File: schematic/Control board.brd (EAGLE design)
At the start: 40.3 x 66 mm, 14 parts, among them IC2 ATTINY44AQFN-20

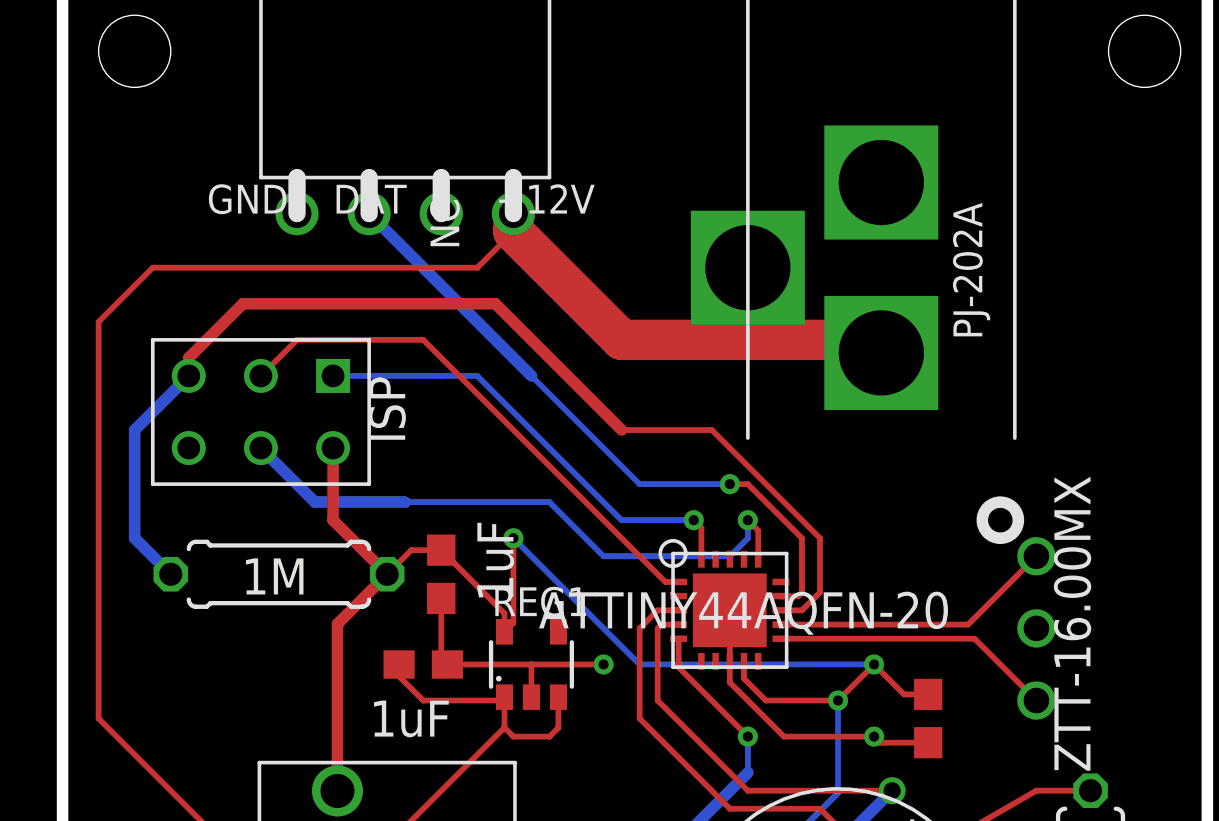
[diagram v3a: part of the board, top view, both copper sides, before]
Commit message: Updated board with QFN-20 microcontroller
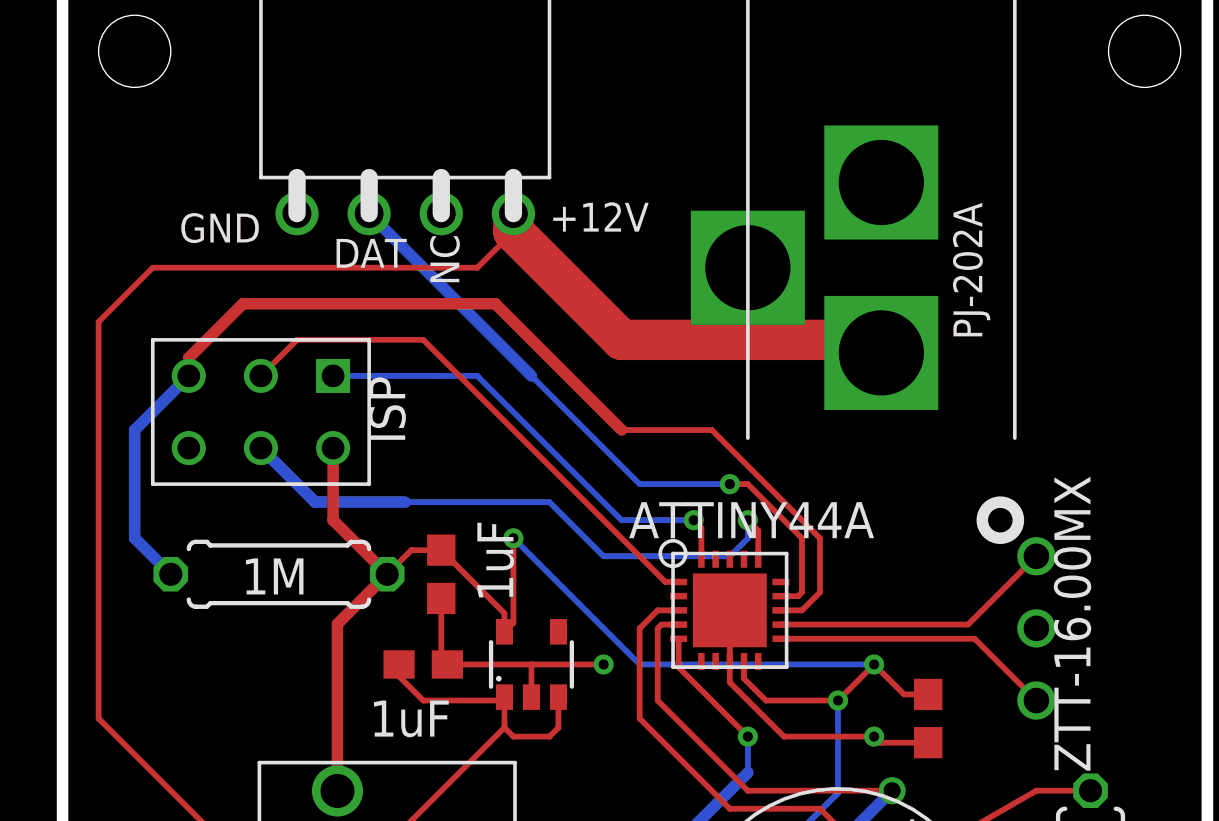
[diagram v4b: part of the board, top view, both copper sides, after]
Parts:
- IC2: value ATTINY44AQFN-20 -> ATTINY44A
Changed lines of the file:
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@@
 <wire x1="40.31" y1="66.03" x2="0" y2="66.03" width="0.4064" layer="20"/>
 <wire x1="0" y1="66.03" x2="0" y2="0" width="0.4064" layer="20"/>
-<text x="15.24" y="57.785" size="1.016" layer="21" font="vector">+12V</text>
-<text x="5.08" y="57.785" size="1.016" layer="21" font="vector">GND</text>
-<text x="9.525" y="57.785" size="1.016" layer="21" font="vector">DAT</text>
-<text x="13.97" y="56.515" size="1.016" layer="21" font="vector" rot="R90">NC</text>
+<text x="17.145" y="57.15" size="1.016" layer="21" font="vector">+12V</text>
+<text x="6.985" y="57.785" size="1.016" layer="21" font="vector" rot="R180">GND</text>
+<text x="9.525" y="55.88" size="1.016" layer="21" font="vector">DAT</text>
+<text x="13.97" y="55.245" size="1.016" layer="21" font="vector" rot="R90">NC</text>
 <circle x="33.02" y="46.99" radius="0.635" width="0.4064" layer="21"/>
 <hole x="2.54" y="63.5" drill="2.54"/>
@@
 </element>
 <element name="CONN1" library="RGB LED project" package="S5440" value="4-PIN-RIGHT-ANGLE" x="12.065" y="57.785" smashed="yes"/>
-<element name="IC2" library="RGB LED project" package="QFN-20" value="ATTINY44AQFN-20" x="23.495" y="43.815" smashed="yes">
-<attribute name="VALUE" x="16.764" y="43.18" size="1.27" layer="21" font="vector" ratio="10"/>
+<element name="IC2" library="RGB LED project" package="QFN-20" value="ATTINY44A" x="23.495" y="43.815" smashed="yes">
+<attribute name="VALUE" x="19.939" y="46.355" size="1.27" layer="21" font="vector" ratio="10"/>
 </element>
 <element name="POW1" library="RGB LED project" package="PJ202A" value="PJ-202A" x="24.13" y="55.88" smashed="yes" rot="R90">
@@
 <attribute name="VALUE" x="31.115" y="33.655" size="1.27" layer="21" font="vector" rot="R90"/>
 </element>
-<element name="REG1" library="RGB LED project" package="SOT-23-5" value="MIC5205" x="16.51" y="41.91"/>
+<element name="REG1" library="RGB LED project" package="SOT-23-5" value="MIC5205" x="16.51" y="41.91" smashed="yes">
+<attribute name="VALUE" x="15.113" y="39.238" size="1.016" layer="27" ratio="10"/>
+</element>
 </elements>
 <signals>

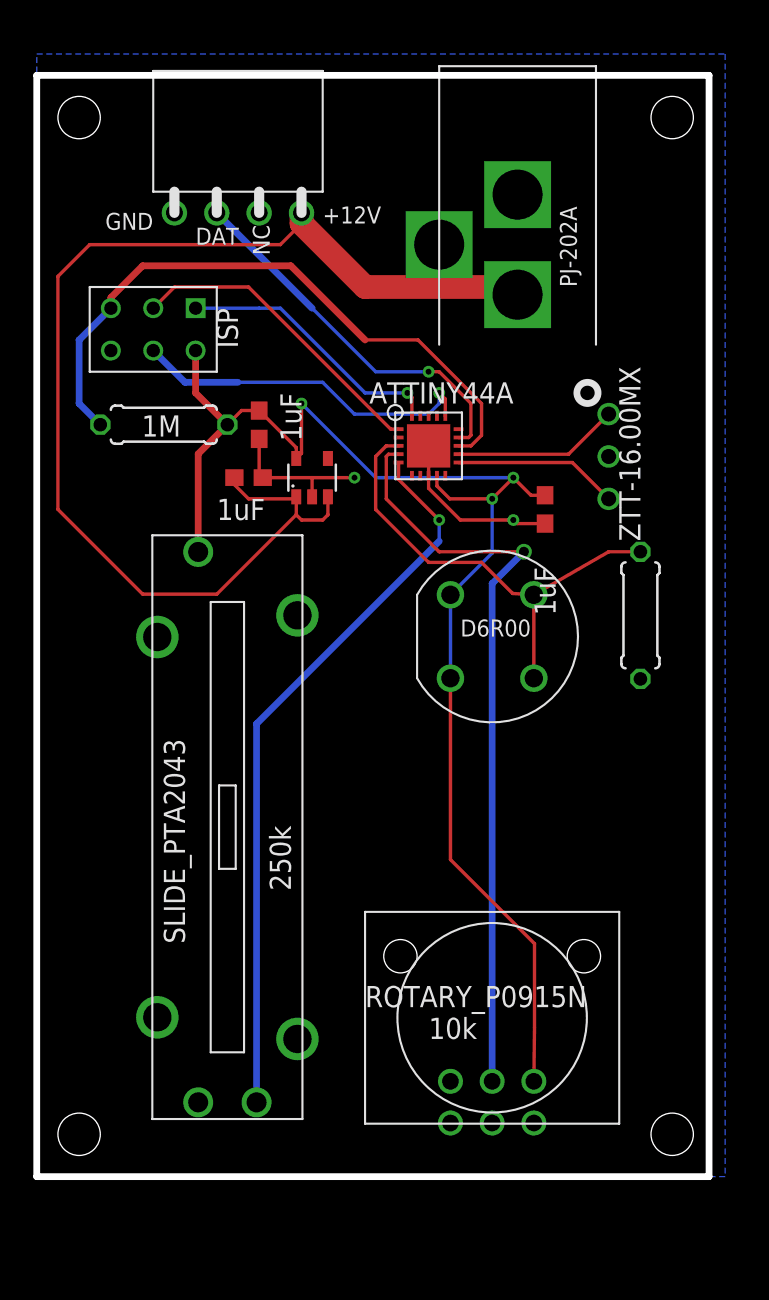
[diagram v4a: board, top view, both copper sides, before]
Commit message: Made the circuit board more compact
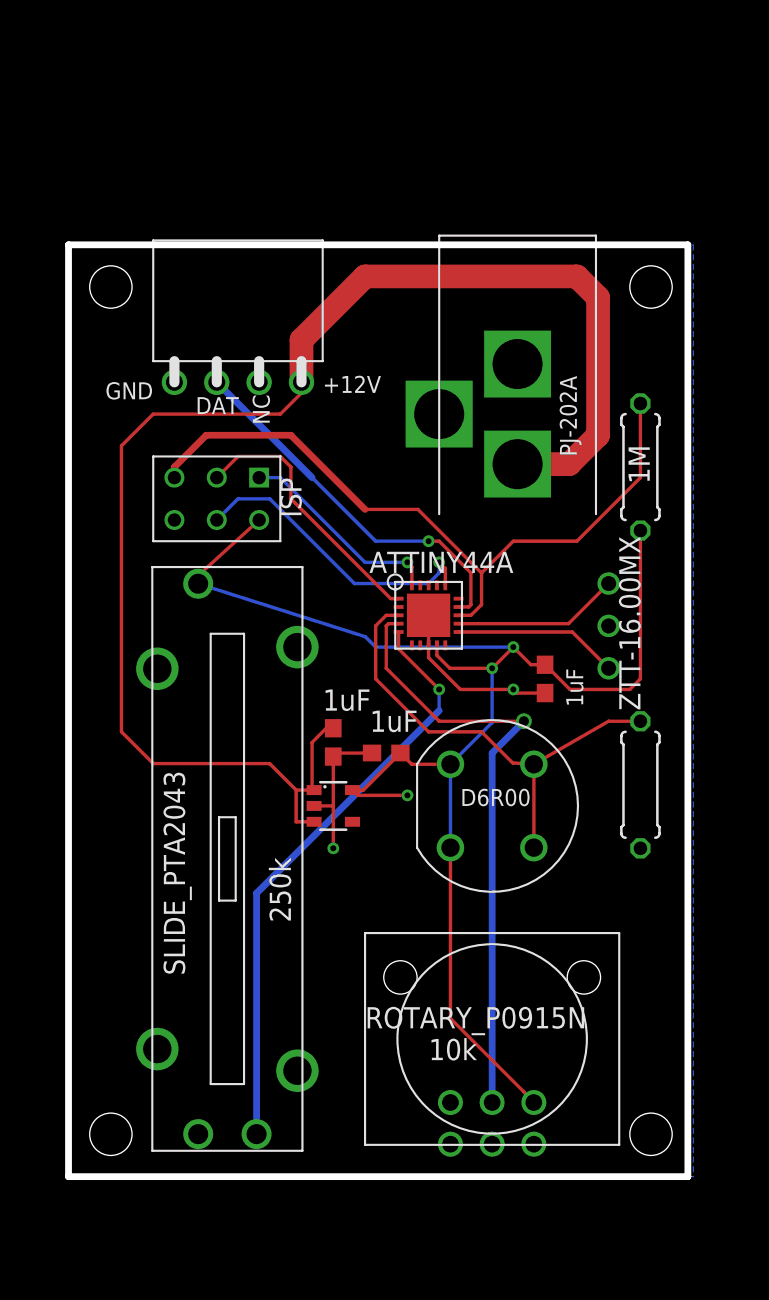
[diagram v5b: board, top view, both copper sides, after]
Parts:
- moved R3 28.7 mm to (36.2, 42.5), turned to 90 degrees
- moved C2 21.1 mm to (21.0, 25.4), turned to 180 degrees
- moved REG1 19.7 mm to (17.8, 22.2), turned to 270 degrees
- moved C1 16.7 mm to (17.8, 26.0), turned to 270 degrees
- moved U$1 10.9 mm to (10.8, 40.6)
- moved C3 10.2 mm to (30.5, 29.8)
- moved POW1 10.2 mm to (24.1, 45.7)
- moved R1 10.2 mm to (36.2, 23.5)
- moved CONN1 10.2 mm to (12.1, 47.6)
- moved IC2 10.2 mm to (23.5, 33.7)
- moved RES1 10.2 mm to (34.3, 33.0)
- moved S1 10.2 mm to (27.3, 22.2)
- moved SLIDE_PTA2043 1.90 mm to (11.4, 19.1)
- moved ROTARY_P0915N 1.27 mm to (27.3, 4.45)
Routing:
- net +12V: track 72.4 -> 86.0 mm
- net ROT_V: track 45.4 -> 36.6 mm
- net SLIDE_V: track 43.9 -> 35.6 mm
- net +5V: track 84.0 -> 88.6 mm
- net RESET: track 38.9 -> 43.1 mm
- net MISO: track 16.3 -> 12.5 mm
- net MOSI: track 21.1 -> 18.4 mm
- net SCK: track 18.8 -> 16.1 mm
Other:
- board size 40.3 x 66 mm -> 37.1 x 55.9 mm
